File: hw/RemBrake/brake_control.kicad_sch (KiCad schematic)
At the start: 33 parts, among them J7 Conn_01x03, J8 Conn_01x07, J9 Conn_01x07, Q8 BC337, Q9 BC847, U5 LM555xN, U6 BD5230G-TR

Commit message: updated schematics and pcb - smd transistor was not connected to resistor to limit current through buzzer
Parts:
- C12: value 680pF -> 0.1uF
- Q8, R42, R45, R48: now not fitted; now left out of the parts list
- Q9, R43, R46: now fitted; now in the parts list
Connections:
- net BUZZER: no longer Q9.3 (C)
- net at Q8.1 (C), R42.1, R46.2: now also Q9.3 (C)
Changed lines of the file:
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@@
 	)
 	(junction
-		(at 260.35 34.29)
-		(diameter 0)
-		(color 0 0 0 0)
-	)
-	(junction
 		(at 72.39 152.4)
 		(diameter 0)
@@
 	(wire
 		(pts
+			(xy 260.35 48.26) (xy 236.22 48.26)
+		)
+		(stroke
+			(width 0)
+			(type default)
+		)
+	)
+	(wire
+		(pts
 			(xy 257.81 142.24) (xy 257.81 156.21)
 		)
@@
 	(wire
 		(pts
-			(xy 260.35 34.29) (xy 260.35 50.8)
-		)
-		(stroke
-			(width 0)
-			(type default)
-		)
-	)
-	(wire
-		(pts
 			(xy 81.28 50.8) (xy 81.28 53.34)
 		)
@@
 	(wire
 		(pts
-			(xy 236.22 34.29) (xy 260.35 34.29)
+			(xy 236.22 34.29) (xy 266.7 34.29)
 		)
 		(stroke
@@
 	(wire
 		(pts
+			(xy 260.35 50.8) (xy 260.35 48.26)
+		)
+		(stroke
+			(width 0)
+			(type default)
+		)
+	)
+	(wire
+		(pts
 			(xy 63.5 157.48) (xy 80.01 157.48)
 		)
@@
 	(wire
 		(pts
-			(xy 260.35 34.29) (xy 266.7 34.29)
-		)
-		(stroke
-			(width 0)
-			(type default)
-		)
-	)
-	(wire
-		(pts
 			(xy 40.64 91.44) (xy 46.99 91.44)
 		)
@@
 		(unit 1)
 		(exclude_from_sim no)
-		(in_bom yes)
+		(in_bom no)
 		(on_board yes)
-		(dnp no)
+		(dnp yes)
 		(fields_autoplaced yes)
 		(property "Reference" "Q8"
@@
 		(unit 1)
 		(exclude_from_sim no)
-		(in_bom yes)
+		(in_bom no)
 		(on_board yes)
-		(dnp no)
+		(dnp yes)
 		(property "Reference" "R42"
 			(at 220.98 45.974 90)
@@
 		(unit 1)
 		(exclude_from_sim no)
-		(in_bom no)
+		(in_bom yes)
 		(on_board yes)
-		(dnp yes)
+		(dnp no)
 		(property "Reference" "R43"
 			(at 220.98 53.594 90)
@@
 		(unit 1)
 		(exclude_from_sim no)
-		(in_bom no)
+		(in_bom yes)
 		(on_board yes)
-		(dnp yes)
+		(dnp no)
 		(fields_autoplaced yes)
 		(property "Reference" "Q9"
@@
 			)
 		)
-		(property "Value" "680pF"
+		(property "Value" "0.1uF"
 			(at 262.128 136.398 0)
 			(effects
@@
 		(unit 1)
 		(exclude_from_sim no)
-		(in_bom no)
+		(in_bom yes)
 		(on_board yes)
-		(dnp yes)
+		(dnp no)
 		(property "Reference" "R46"
 			(at 238.506 40.64 90)
@@
 		(unit 1)
 		(exclude_from_sim no)
-		(in_bom yes)
+		(in_bom no)
 		(on_board yes)
-		(dnp no)
+		(dnp yes)
 		(property "Reference" "R48"
 			(at 252.73 65.024 90)
@@
 		(unit 1)
 		(exclude_from_sim no)
-		(in_bom yes)
+		(in_bom no)
 		(on_board yes)
-		(dnp no)
+		(dnp yes)
 		(property "Reference" "R45"
 			(at 226.314 40.64 90)

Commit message: removed hopefully last redundant components and updated versions of pcb and schematics
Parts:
- R35: now left out of the parts list
- R37, R40: now in the parts list

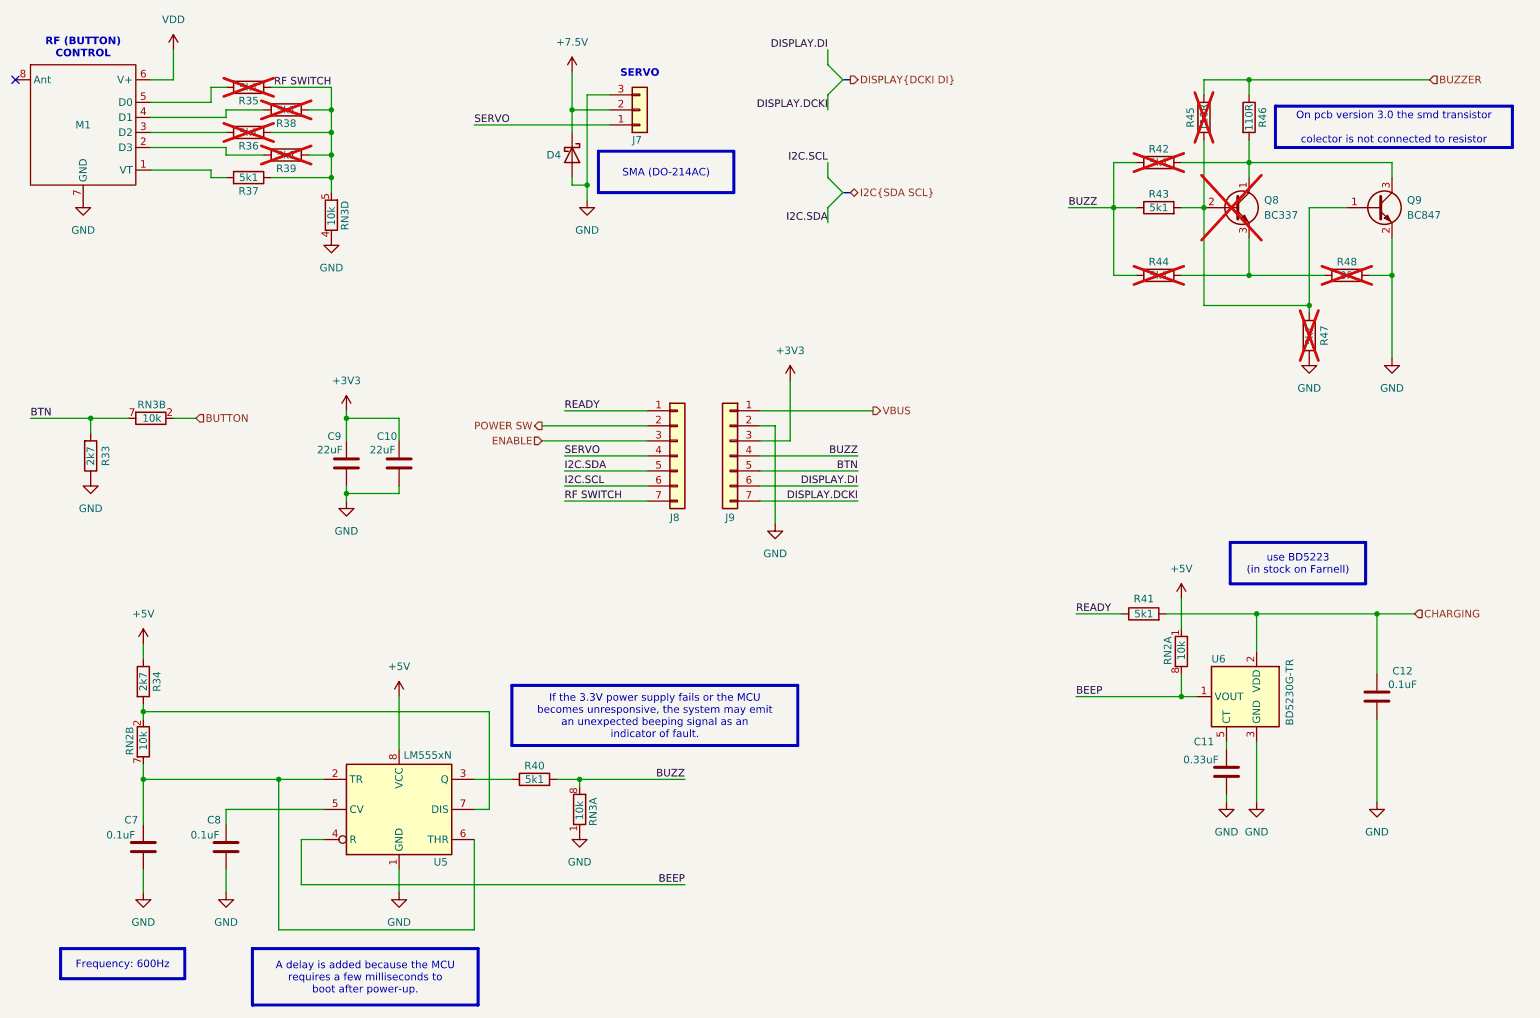
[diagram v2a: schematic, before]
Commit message: updated pcb and added Notes about possible faults
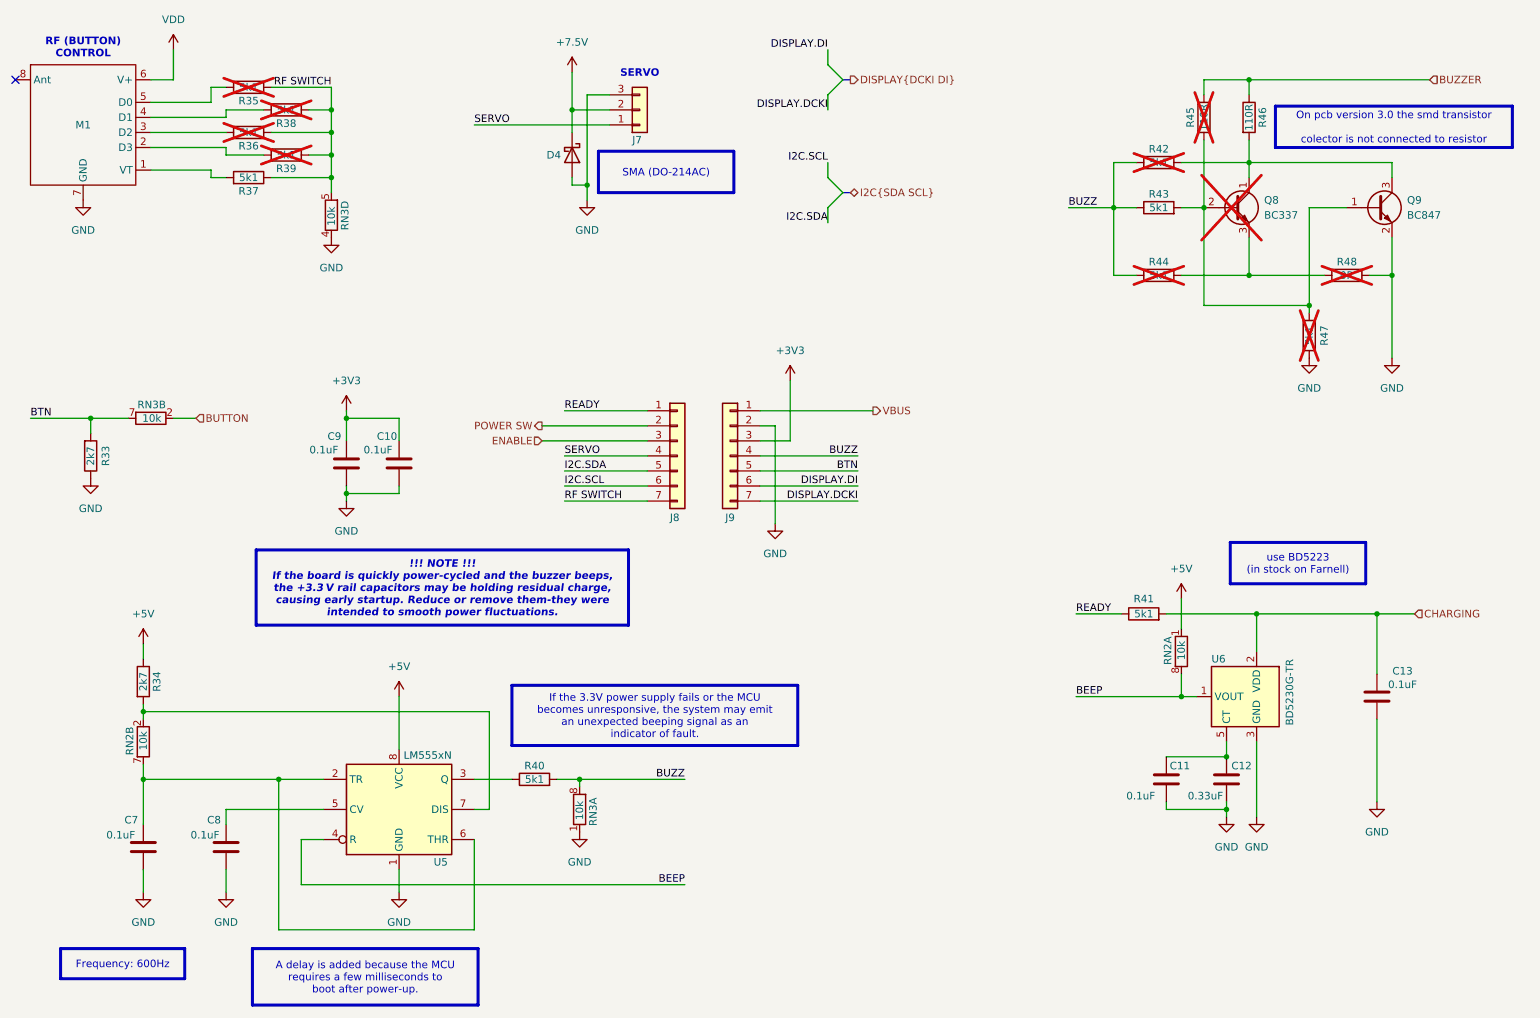
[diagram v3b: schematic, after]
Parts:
- added C11: 0.1uF, Capacitor_SMD:C_0805_2012Metric_Pad1.18x1.45mm_HandSolder, symbol Device:C
- C10, C9: value 22uF -> 0.1uF
- renumbered C11 to C12, C12 to C13
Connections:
- net GND: now also C11.2
- net at C12.1, U6.5 (CT): now also C11.1
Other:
- moved on the sheet: C12
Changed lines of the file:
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@@
 		)
 	)
+	(text_box "!!! NOTE !!!\nIf the board is quickly power-cycled and the buzzer beeps, the +3.3 V rail capacitors may be holding residual charge, causing early startup. Reduce or remove them-they were intended to smooth power fluctuations."
+		(exclude_from_sim no)
+		(at 68.58 113.665 0)
+		(size 62.865 12.7)
+		(margins 0.9525 0.9525 0.9525 0.9525)
+		(stroke
+			(width 0.508)
+			(type solid)
+			(color 128 63 0 1)
+		)
+		(fill
+			(type color)
+			(color 255 255 153 1)
+		)
+		(effects
+			(font
+				(size 1.27 1.27)
+				(thickness 0.254)
+				(bold yes)
+				(italic yes)
+			)
+		)
+	)
 	(text_box "A delay is added because the MCU\nrequires a few milliseconds to \nboot after power-up."
 		(exclude_from_sim no)
@@
 	)
 	(junction
+		(at 232.41 157.48)
+		(diameter 0)
+		(color 0 0 0 0)
+	)
+	(junction
 		(at 121.92 39.37)
 		(diameter 0)
@@
 	)
 	(junction
+		(at 232.41 148.59)
+		(diameter 0)
+		(color 0 0 0 0)
+	)
+	(junction
 		(at 257.81 124.46)
 		(diameter 0)
@@
 	(wire
 		(pts
-			(xy 237.49 156.21) (xy 237.49 146.05)
+			(xy 237.49 158.75) (xy 237.49 146.05)
 		)
 		(stroke
@@
 	(wire
 		(pts
+			(xy 222.25 157.48) (xy 232.41 157.48)
+		)
+		(stroke
+			(width 0)
+			(type default)
+		)
+	)
+	(wire
+		(pts
 			(xy 71.12 43.18) (xy 81.28 43.18)
 		)
@@
 	(wire
 		(pts
+			(xy 222.25 148.59) (xy 232.41 148.59)
+		)
+		(stroke
+			(width 0)
+			(type default)
+		)
+	)
+	(wire
+		(pts
 			(xy 63.5 45.72) (xy 63.5 46.99)
 		)
@@
 	(wire
 		(pts
-			(xy 232.41 146.05) (xy 232.41 147.32)
+			(xy 232.41 146.05) (xy 232.41 148.59)
 		)
 		(stroke
@@
 	(wire
 		(pts
-			(xy 232.41 154.94) (xy 232.41 156.21)
+			(xy 232.41 156.21) (xy 232.41 157.48)
 		)
 		(stroke
@@
 	(wire
 		(pts
+			(xy 232.41 157.48) (xy 232.41 158.75)
+		)
+		(stroke
+			(width 0)
+			(type default)
+		)
+	)
+	(wire
+		(pts
 			(xy 49.53 167.64) (xy 49.53 171.45)
 		)
@@
 	(wire
 		(pts
+			(xy 222.25 156.21) (xy 222.25 157.48)
+		)
+		(stroke
+			(width 0)
+			(type default)
+		)
+	)
+	(wire
+		(pts
 			(xy 40.64 91.44) (xy 46.99 91.44)
 		)
@@
 			)
 		)
-		(property "Value" "22uF"
-			(at 81.026 96.774 0)
+		(property "Value" "0.1uF"
+			(at 80.01 96.774 0)
 			(effects
 				(font
@@
 		(on_board yes)
 		(dnp no)
-		(property "Reference" "C12"
+		(property "Reference" "C13"
 			(at 262.128 134.112 0)
 			(effects
@@
 			(project "RemBrake"
 				(path "/e6d4ae5b-c9d7-4cbe-b288-c929fdf55a75/4813b76c-f465-42f9-8515-5ce5d55b4403"
-					(reference "C12")
+					(reference "C13")
 					(unit 1)
 				)
@@
 	(symbol
 		(lib_id "power:GND")
-		(at 232.41 156.21 0)
+		(at 232.41 158.75 0)
 		(mirror y)
 		(unit 1)
@@
 		(fields_autoplaced yes)
 		(property "Reference" "#PWR060"
-			(at 232.41 162.56 0)
+			(at 232.41 165.1 0)
 			(hide yes)
 			(effects
@@
 		)
 		(property "Value" "GND"
-			(at 232.41 161.29 0)
+			(at 232.41 163.83 0)
 			(effects
 				(font
@@
 		)
 		(property "Footprint" ""
-			(at 232.41 156.21 0)
+			(at 232.41 158.75 0)
 			(hide yes)
 			(effects
@@
 		)
 		(property "Datasheet" ""
-			(at 232.41 156.21 0)
+			(at 232.41 158.75 0)
 			(hide yes)
 			(effects
@@
 		)
 		(property "Description" "Power symbol creates a global label with name \"GND\" , ground"
-			(at 232.41 156.21 0)
+			(at 232.41 158.75 0)
 			(hide yes)
 			(effects
@@
 			)
 		)
-		(property "Value" "22uF"
-			(at 89.916 96.774 0)
+		(property "Value" "0.1uF"
+			(at 89.154 96.774 0)
 			(effects
 				(font
@@
 	)
 	(symbol
+		(lib_id "Device:C")
+		(at 222.25 152.4 0)
+		(unit 1)
+		(exclude_from_sim no)
+		(in_bom yes)
+		(on_board yes)
+		(dnp no)
+		(property "Reference" "C11"
+			(at 224.536 150.114 0)
+			(effects
+				(font
+					(size 1.27 1.27)
+				)
+			)
+		)
+		(property "Value" "0.1uF"
+			(at 217.932 155.194 0)
+			(effects
+				(font
+					(size 1.27 1.27)
+				)
+			)
+		)
+		(property "Footprint" "Capacitor_SMD:C_0805_2012Metric_Pad1.18x1.45mm_HandSolder"
+			(at 223.2152 156.21 0)
+			(hide yes)
+			(effects
+				(font
+					(size 1.27 1.27)
+				)
+			)
+		)
+		(property "Datasheet" ""
+			(at 222.25 152.4 0)
+			(hide yes)
+			(effects
+				(font
+					(size 1.27 1.27)
+				)
+			)
+		)
+		(property "Description" "Unpolarized capacitor"
+			(at 222.25 152.4 0)
+			(hide yes)
+			(effects
+				(font
+					(size 1.27 1.27)
+				)
+			)
+		)
+		(property "Purchase" ""
+			(at 222.25 152.4 0)
+			(hide yes)
+			(effects
+				(font
+					(size 1.27 1.27)
+				)
+			)
+		)
+		(pin "2"
+		)
+		(pin "1"
+		)
+		(instances
+			(project "RemBrake"
+				(path "/e6d4ae5b-c9d7-4cbe-b288-c929fdf55a75/4813b76c-f465-42f9-8515-5ce5d55b4403"
+					(reference "C11")
+					(unit 1)
+				)
+			)
+		)
+	)
+	(symbol
 		(lib_id "power:GND")
 		(at 156.21 109.22 0)
@@
 	(symbol
 		(lib_id "power:GND")
-		(at 237.49 156.21 0)
+		(at 237.49 158.75 0)
 		(mirror y)
 		(unit 1)
@@
 		(fields_autoplaced yes)
 		(property "Reference" "#PWR061"
-			(at 237.49 162.56 0)
+			(at 237.49 165.1 0)
 			(hide yes)
 			(effects
@@
 		)
 		(property "Value" "GND"
-			(at 237.49 161.29 0)
+			(at 237.49 163.83 0)
 			(effects
 				(font
@@
 		)
 		(property "Footprint" ""
-			(at 237.49 156.21 0)
+			(at 237.49 158.75 0)
 			(hide yes)
 			(effects
@@
 		)
 		(property "Datasheet" ""
-			(at 237.49 156.21 0)
+			(at 237.49 158.75 0)
 			(hide yes)
 			(effects
@@
 		)
 		(property "Description" "Power symbol creates a global label with name \"GND\" , ground"
-			(at 237.49 156.21 0)
+			(at 237.49 158.75 0)
 			(hide yes)
 			(effects
@@
 	(symbol
 		(lib_id "Device:C")
-		(at 232.41 151.13 0)
+		(at 232.41 152.4 0)
 		(unit 1)
 		(exclude_from_sim no)
@@
 		(on_board yes)
 		(dnp no)
-		(property "Reference" "C11"
-			(at 228.6 146.05 0)
+		(property "Reference" "C12"
+			(at 234.95 150.114 0)
 			(effects
 				(font
@@
 		)
 		(property "Value" "0.33uF"
-			(at 228.092 149.098 0)
+			(at 228.854 155.194 0)
 			(effects
 				(font
@@
 		)
 		(property "Footprint" "Capacitor_SMD:C_0805_2012Metric_Pad1.18x1.45mm_HandSolder"
-			(at 233.3752 154.94 0)
+			(at 233.3752 156.21 0)
 			(hide yes)
 			(effects
@@
 		)
 		(property "Datasheet" ""
-			(at 232.41 151.13 0)
+			(at 232.41 152.4 0)
 			(hide yes)
 			(effects
@@
 		)
 		(property "Description" "Unpolarized capacitor"
-			(at 232.41 151.13 0)
+			(at 232.41 152.4 0)
 			(hide yes)
 			(effects
@@
 		)
 		(property "Purchase" ""
-			(at 232.41 151.13 0)
+			(at 232.41 152.4 0)
 			(hide yes)
 			(effects
@@
 			(project "RemBrake"
 				(path "/e6d4ae5b-c9d7-4cbe-b288-c929fdf55a75/4813b76c-f465-42f9-8515-5ce5d55b4403"
-					(reference "C11")
+					(reference "C12")
 					(unit 1)
 				)

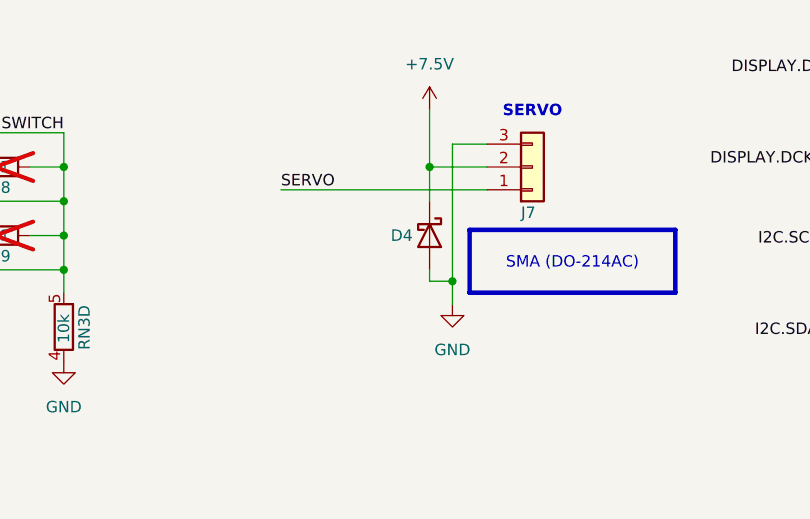
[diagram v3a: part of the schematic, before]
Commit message: added protection diode at the power input
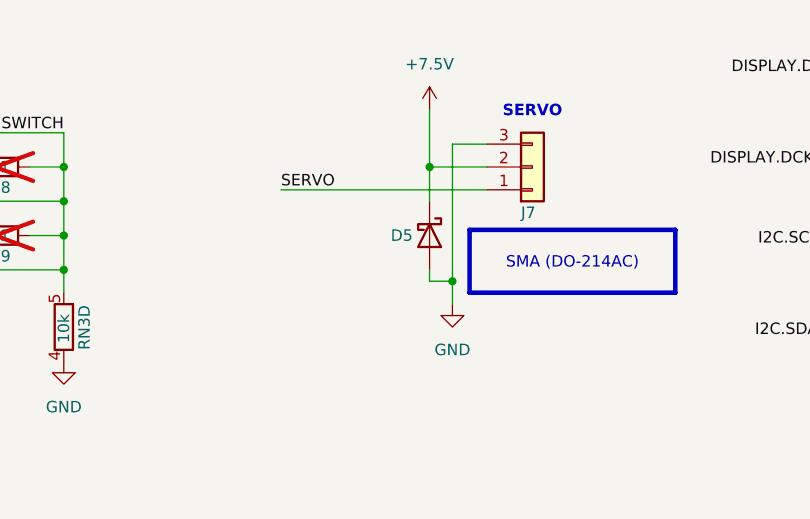
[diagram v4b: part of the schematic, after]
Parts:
- renumbered D4 to D5
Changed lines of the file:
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@@
 (kicad_sch
-	(version 20250513)
+	(version 20250610)
 	(generator "eeschema")
 	(generator_version "9.99")
@@
 		(on_board yes)
 		(dnp no)
-		(property "Reference" "D4"
+		(property "Reference" "D5"
 			(at 117.602 46.99 90)
 			(effects
@@
 			(project ""
 				(path "/e6d4ae5b-c9d7-4cbe-b288-c929fdf55a75/4813b76c-f465-42f9-8515-5ce5d55b4403"
-					(reference "D4")
+					(reference "D5")
 					(unit 1)
 				)
